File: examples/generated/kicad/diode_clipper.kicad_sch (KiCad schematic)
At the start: 3 parts

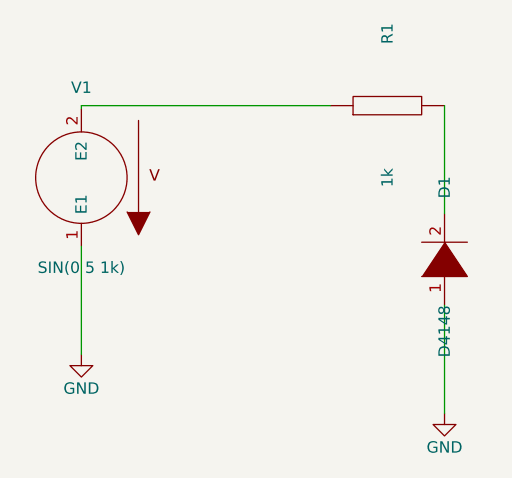
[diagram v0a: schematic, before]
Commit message: Ensure connectivity matches, as measured by opamp connectivity.
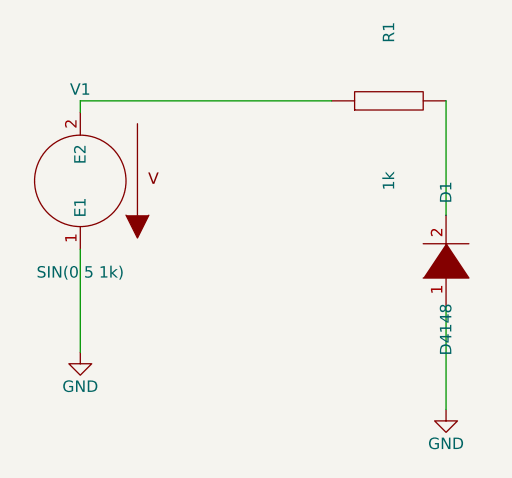
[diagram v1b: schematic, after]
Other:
- moved on the sheet: R1
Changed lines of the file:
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@@
     (comment 1 "Generated by mixedsig2cad")
   )
-  (symbol (lib_id "VSOURCE") (at 56.00 86.00 180) (unit 1)
+  (symbol (lib_id "VSOURCE") (at 55.88 86.36 180) (unit 1)
     (in_bom yes) (on_board yes)
-    (property "Reference" "V1" (at 56.0 76.0 0)
+    (property "Reference" "V1" (at 55.88 76.2 0)
       (effects (font (size 1.27 1.27)))
     )
-    (property "Value" "SIN(0 5 1k)" (at 56.0 96.0 0)
+    (property "Value" "SIN(0 5 1k)" (at 55.88 96.52 0)
       (effects (font (size 1.27 1.27)))
     )
@@
     )
   )
-  (symbol (lib_id "GND") (at 56.00 105.62 0) (unit 1)
+  (symbol (lib_id "GND") (at 55.88 105.41 0) (unit 1)
     (in_bom yes) (on_board yes)
-    (property "Reference" "#PWR0001" (at 56.0 101.81 0)
+    (property "Reference" "#PWR0001" (at 55.88 101.6 0)
       (effects (font (size 1.27 1.27)) hide)
     )
-    (property "Value" "GND" (at 56.0 109.43 0)
+    (property "Value" "GND" (at 55.88 109.22 0)
       (effects (font (size 1.27 1.27)))
     )
@@
     )
   )
-  (symbol (lib_id "R") (at 90.00 78.00 90) (unit 1)
+  (symbol (lib_id "R") (at 90.17 77.47 90) (unit 1)
     (in_bom yes) (on_board yes)
-    (property "Reference" "R1" (at 90.0 70.0 0)
+    (property "Reference" "R1" (at 90.17 69.85 0)
       (effects (font (size 1.27 1.27)))
     )
-    (property "Value" "1k" (at 90.0 86.0 0)
+    (property "Value" "1k" (at 90.17 86.36 0)
       (effects (font (size 1.27 1.27)))
     )
@@
     )
   )
-  (symbol (lib_id "DIODE") (at 96.35 95.08 90) (unit 1)
+  (symbol (lib_id "DIODE") (at 96.52 95.25 90) (unit 1)
     (in_bom yes) (on_board yes)
-    (property "Reference" "D1" (at 96.35 87.08 0)
+    (property "Reference" "D1" (at 96.52 87.63 0)
       (effects (font (size 1.27 1.27)))
     )
-    (property "Value" "D4148" (at 96.35 103.08 0)
+    (property "Value" "D4148" (at 96.52 102.87 0)
       (effects (font (size 1.27 1.27)))
     )
@@
     )
   )
-  (symbol (lib_id "GND") (at 96.35 112.16 0) (unit 1)
+  (symbol (lib_id "GND") (at 96.52 111.76 0) (unit 1)
     (in_bom yes) (on_board yes)
-    (property "Reference" "#PWR0002" (at 96.35 108.35 0)
+    (property "Reference" "#PWR0002" (at 96.52 107.95 0)
       (effects (font (size 1.27 1.27)) hide)
     )
-    (property "Value" "GND" (at 96.35 115.97 0)
+    (property "Value" "GND" (at 96.52 115.57000000000001 0)
       (effects (font (size 1.27 1.27)))
     )
@@
     )
   )
-  (wire (pts (xy 96.35 100.16) (xy 96.35 112.16))
+  (wire (pts (xy 96.52 100.33) (xy 96.52 111.76))
     (stroke (width 0) (type solid) (color 0 0 0 0))
   )
-  (wire (pts (xy 56.00 93.62) (xy 56.00 105.62))
+  (wire (pts (xy 55.88 93.98) (xy 55.88 105.41))
     (stroke (width 0) (type solid) (color 0 0 0 0))
   )
-  (wire (pts (xy 56.00 78.38) (xy 56.00 78.00))
+  (wire (pts (xy 55.88 78.74) (xy 55.88 77.47))
     (stroke (width 0) (type solid) (color 0 0 0 0))
   )
-  (wire (pts (xy 56.00 78.00) (xy 83.65 78.00))
+  (wire (pts (xy 55.88 77.47) (xy 83.82 77.47))
     (stroke (width 0) (type solid) (color 0 0 0 0))
   )
-  (wire (pts (xy 96.35 78.00) (xy 96.35 90.00))
+  (wire (pts (xy 96.52 77.47) (xy 96.52 90.17))
     (stroke (width 0) (type solid) (color 0 0 0 0))
   )

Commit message: Refactor further.
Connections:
- net vin: now reaches R1.1, V1.2 (E2)
- net vout: now reaches D1.2 (A), R1.2
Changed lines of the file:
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@@
     )
+  )
+  (label "vin" (at 69.85 77.47 0)
+    (effects (font (size 1.27 1.27)))
+  )
+  (label "vout" (at 96.52 77.47 0)
+    (effects (font (size 1.27 1.27)))
   )
   (wire (pts (xy 96.52 100.33) (xy 96.52 111.76))

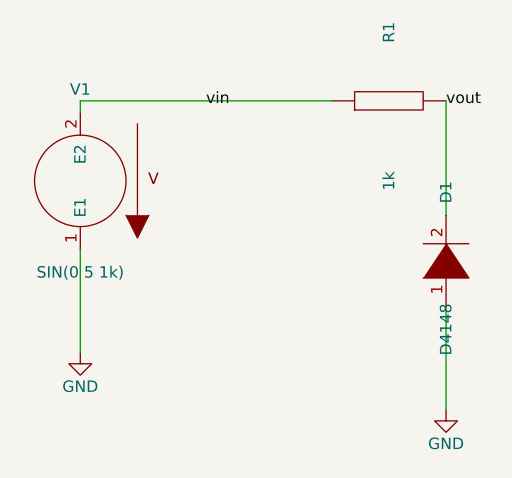
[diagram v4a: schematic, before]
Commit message: Fix CMOS inverter issue.
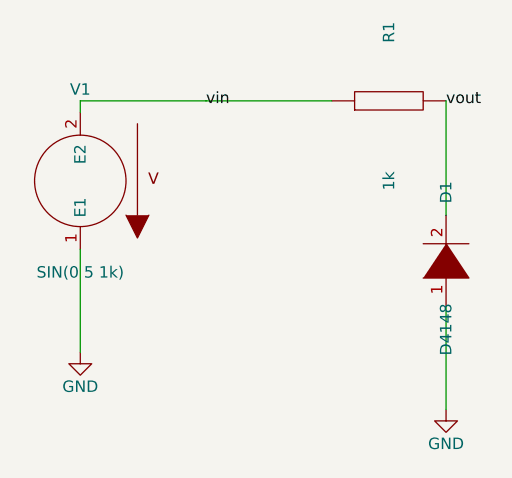
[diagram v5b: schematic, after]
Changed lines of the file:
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@@
     (stroke (width 0) (type solid) (color 0 0 0 0))
   )
-  (wire (pts (xy 55.88 77.47) (xy 83.82 77.47))
+  (wire (pts (xy 55.88 77.47) (xy 69.85 77.47))
     (stroke (width 0) (type solid) (color 0 0 0 0))
   )
-  (wire (pts (xy 96.52 77.47) (xy 96.52 90.17))
+  (wire (pts (xy 83.82 77.47) (xy 69.85 77.47))
     (stroke (width 0) (type solid) (color 0 0 0 0))
   )
+  (wire (pts (xy 96.52 90.17) (xy 96.52 77.47))
+    (stroke (width 0) (type solid) (color 0 0 0 0))
+  )

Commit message: Manually change schematics to match what I want.
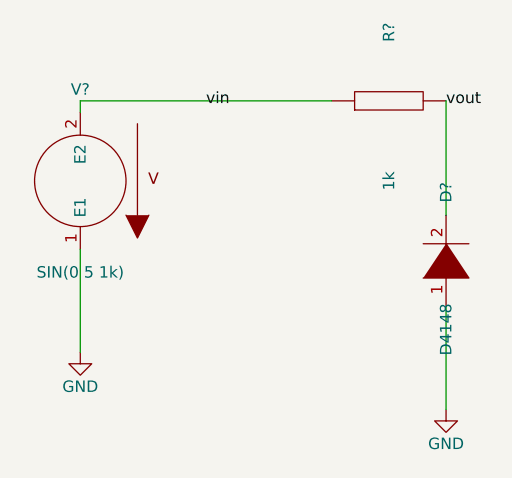
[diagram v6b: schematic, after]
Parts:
- renumbered D1 to D?, R1 to R?, V1 to V?

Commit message: Attempt to match manual schematics with seeded layout and generation.
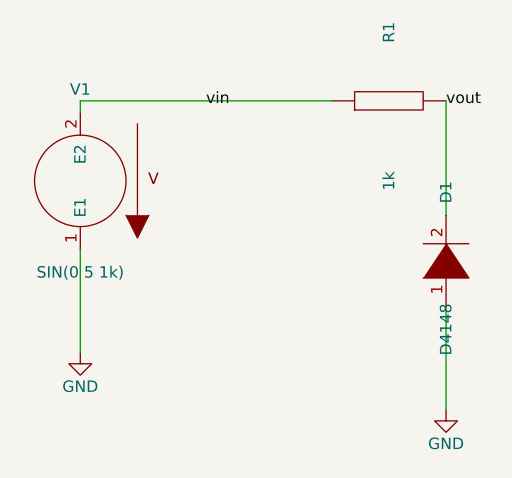
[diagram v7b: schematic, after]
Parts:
- gave numbers to parts that had none: 3
